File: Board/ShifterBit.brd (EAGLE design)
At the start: 27.2 x 61 mm, 13 parts

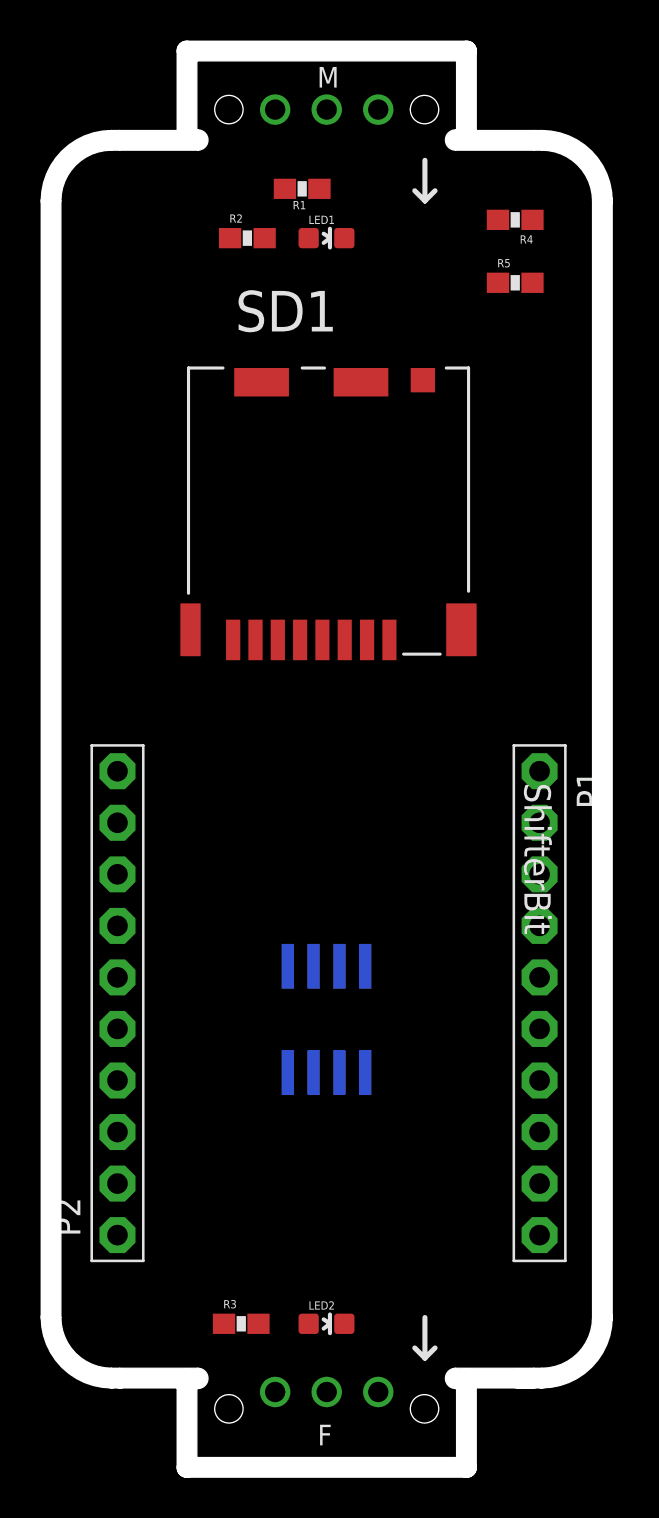
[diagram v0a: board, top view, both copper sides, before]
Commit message: corrected socket position
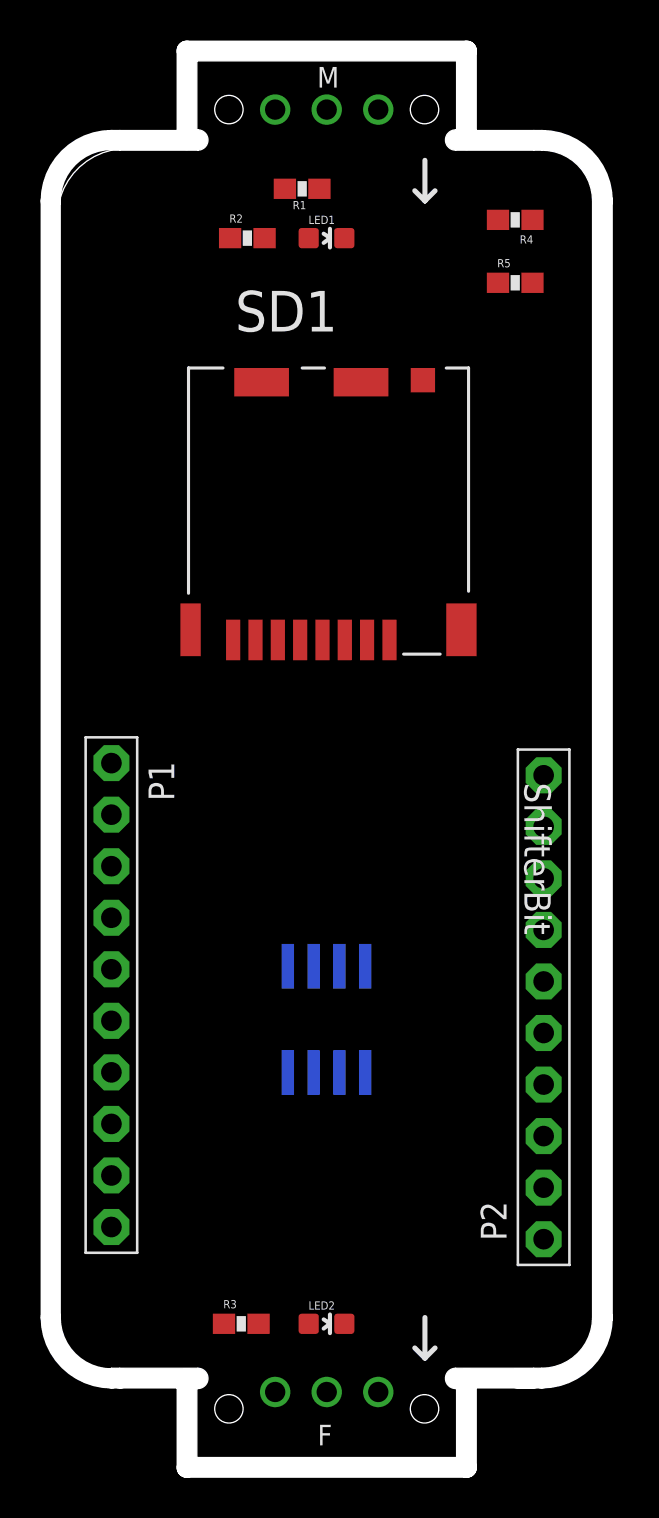
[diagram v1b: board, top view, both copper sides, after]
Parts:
- moved P1 21.1 mm to (2.60, 23.0)
- moved P2 21.0 mm to (23.9, 22.4)
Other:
- outline, holes or cut-outs redrawn
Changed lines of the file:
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@@
 <board>
 <plain>
-<wire x1="0.11" y1="62.135" x2="0.11" y2="7.11" width="0" layer="20"/>
-<wire x1="0.11" y1="7.11" x2="2.61" y2="4.61" width="0" layer="20" curve="90"/>
+<wire x1="0.01" y1="60.535" x2="0.01" y2="5.51" width="0" layer="20"/>
+<wire x1="0.01" y1="5.51" x2="2.61" y2="4.61" width="0" layer="20" curve="90"/>
 <wire x1="2.61" y1="4.61" x2="3.01" y2="4.61" width="0" layer="20"/>
-<wire x1="0.11" y1="62.135" x2="2.61" y2="64.635" width="0" layer="20" curve="-90"/>
+<wire x1="0.01" y1="60.535" x2="2.61" y2="64.635" width="0" layer="20" curve="-90"/>
 <wire x1="2.61" y1="64.635" x2="3.01" y2="64.635" width="0" layer="20"/>
 <wire x1="23.41" y1="64.635" x2="23.81" y2="64.635" width="0" layer="20"/>
@@
 <element name="BSF1" library="bitSnap" package="BITSNAP_V03_FEMALE" value="BITSNAP_V03_FEMALE" x="6.605" y="0" locked="yes"/>
 <element name="BSM1" library="bitSnap" package="BITSNAP_V03_MALE" value="BITSNAP_V03_MALE" x="19.815" y="69.245" rot="R180"/>
-<element name="P1" library="adafruit" package="1X10-BIG" value="" x="23.7" y="22.6" rot="R270"/>
-<element name="P2" library="adafruit" package="1X10-BIG" value="" x="2.9" y="22.6" rot="R90"/>
+<element name="P1" library="adafruit" package="1X10-BIG" value="" x="2.6" y="23" rot="R270"/>
+<element name="P2" library="adafruit" package="1X10-BIG" value="" x="23.9" y="22.4" rot="R90"/>
 <element name="SD1" library="HIROSE-DM3CS-SF" package="HIROSE_DM3CS-SF" value="" x="16.3" y="40.5">
 <attribute name="OC_NEWARK" value="35R0581" x="16.3" y="40.5" size="1.778" layer="27" display="off"/>
@@
 <wire x1="14.077" y1="6.8" x2="12.565" y2="19.1838" width="0" layer="19" extent="1-16"/>
 <wire x1="10.67" y1="3.44" x2="14.077" y2="6.8" width="0" layer="19" extent="1-1"/>
-<wire x1="23.7" y1="11.17" x2="14.077" y2="6.8" width="0" layer="19" extent="1-1"/>
-<wire x1="2.9" y1="11.17" x2="10.67" y2="3.44" width="0" layer="19" extent="1-1"/>
+<wire x1="2.6" y1="11.57" x2="14.077" y2="6.8" width="0" layer="19" extent="1-1"/>
+<wire x1="23.9" y1="10.97" x2="10.67" y2="3.44" width="0" layer="19" extent="1-1"/>
 </signal>
 <signal name="VCC">
@@
 <contactref element="R4" pad="1"/>
 <wire x1="23.35" y1="58.1" x2="23.35" y2="61.2" width="0" layer="19" extent="1-1"/>
-<wire x1="23.7" y1="31.49" x2="23.35" y2="58.1" width="0" layer="19" extent="1-1"/>
+<wire x1="2.6" y1="31.89" x2="23.35" y2="58.1" width="0" layer="19" extent="1-1"/>
 </signal>
 <signal name="EN">
@@
 <contactref element="P1" pad="4"/>
 <contactref element="DPOT1" pad="1"/>
-<wire x1="11.295" y1="24.4162" x2="23.7" y2="26.41" width="0" layer="19" extent="16-16"/>
+<wire x1="11.295" y1="24.4162" x2="2.6" y2="26.81" width="0" layer="19" extent="16-16"/>
 </signal>
 <signal name="D14">
@@
 <contactref element="DPOT1" pad="2"/>
 <wire x1="12.565" y1="24.4162" x2="11.9" y2="40.5" width="0" layer="19" extent="1-16"/>
-<wire x1="23.7" y1="23.87" x2="12.565" y2="24.4162" width="0" layer="19" extent="16-16"/>
+<wire x1="2.6" y1="24.27" x2="12.565" y2="24.4162" width="0" layer="19" extent="16-16"/>
 </signal>
 <signal name="D12">
 <contactref element="P1" pad="6"/>
 <contactref element="SD1" pad="7"/>
-<wire x1="23.7" y1="21.33" x2="9.7" y2="40.5" width="0" layer="19" extent="1-1"/>
+<wire x1="2.6" y1="21.73" x2="9.7" y2="40.5" width="0" layer="19" extent="1-1"/>
 </signal>
 <signal name="D13">
@@
 <contactref element="DPOT1" pad="3"/>
 <wire x1="13.835" y1="24.4162" x2="14.1" y2="40.5" width="0" layer="19" extent="1-16"/>
-<wire x1="23.7" y1="18.79" x2="13.835" y2="24.4162" width="0" layer="19" extent="16-16"/>
+<wire x1="2.6" y1="19.19" x2="13.835" y2="24.4162" width="0" layer="19" extent="16-16"/>
 </signal>
 <signal name="V+">
@@
 <contactref element="P2" pad="8"/>
 <contactref element="R2" pad="1"/>
-<wire x1="2.9" y1="28.95" x2="8.45" y2="60.3" width="0" layer="19" extent="1-1"/>
+<wire x1="23.9" y1="28.75" x2="8.45" y2="60.3" width="0" layer="19" extent="1-1"/>
 </signal>
 <signal name="D4">
 <contactref element="P2" pad="7"/>
 <contactref element="R3" pad="1"/>
-<wire x1="8.15" y1="6.8" x2="2.9" y2="26.41" width="0" layer="19" extent="1-1"/>
+<wire x1="8.15" y1="6.8" x2="23.9" y2="26.21" width="0" layer="19" extent="1-1"/>
 </signal>
 <signal name="D0">
@@
 <contactref element="P2" pad="4"/>
 <contactref element="SD1" pad="2"/>
-<wire x1="2.9" y1="18.79" x2="15.2" y2="40.5" width="0" layer="19" extent="1-1"/>
+<wire x1="23.9" y1="18.59" x2="15.2" y2="40.5" width="0" layer="19" extent="1-1"/>
 </signal>
 <signal name="3V">
@@
 <contactref element="DPOT1" pad="8"/>
 <wire x1="11.295" y1="19.1838" x2="13" y2="40.5" width="0" layer="19" extent="1-16"/>
-<wire x1="2.9" y1="16.25" x2="11.295" y2="19.1838" width="0" layer="19" extent="16-16"/>
+<wire x1="23.9" y1="16.05" x2="11.295" y2="19.1838" width="0" layer="19" extent="16-16"/>
 </signal>
 <signal name="LD0">

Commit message: added some aesthetics
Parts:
- R4: value 2K2 -> 3K3
- R5: value 560 -> 820
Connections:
- net 3V: no longer DPOT1.8
- net VCC: now also DPOT1.8
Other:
- outline, holes or cut-outs redrawn
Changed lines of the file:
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@@
 <layer number="47" name="Measures" color="7" fill="1" visible="yes" active="yes"/>
 <layer number="48" name="Document" color="7" fill="1" visible="yes" active="yes"/>
-<layer number="49" name="Reference" color="10" fill="1" visible="yes" active="yes"/>
+<layer number="49" name="Reference" color="10" fill="1" visible="no" active="yes"/>
 <layer number="50" name="dxf" color="7" fill="1" visible="yes" active="yes"/>
 <layer number="51" name="tDocu" color="6" fill="1" visible="yes" active="yes"/>
@@
 <board>
 <plain>
-<wire x1="0.01" y1="60.535" x2="0.01" y2="5.51" width="0" layer="20"/>
-<wire x1="0.01" y1="5.51" x2="2.61" y2="4.61" width="0" layer="20" curve="90"/>
-<wire x1="2.61" y1="4.61" x2="3.01" y2="4.61" width="0" layer="20"/>
-<wire x1="0.01" y1="60.535" x2="2.61" y2="64.635" width="0" layer="20" curve="-90"/>
+<wire x1="0.11" y1="62.035" x2="0.11" y2="6.81" width="0" layer="20"/>
+<wire x1="0.11" y1="6.81" x2="3.01" y2="4.61" width="0" layer="20" curve="90"/>
+<wire x1="0.11" y1="62.035" x2="2.61" y2="64.635" width="0" layer="20" curve="-90"/>
 <wire x1="2.61" y1="64.635" x2="3.01" y2="64.635" width="0" layer="20"/>
 <wire x1="23.41" y1="64.635" x2="23.81" y2="64.635" width="0" layer="20"/>
@@
 <element name="R2" library="SparkFun-Passives" package="0603-RES" value="56" x="9.3" y="60.3"/>
 <element name="R3" library="SparkFun-Passives" package="0603-RES" value="56" x="9" y="6.8"/>
-<element name="R4" library="SparkFun-Passives" package="0603-RES" value="2K2" x="22.5" y="61.2" rot="R180"/>
-<element name="R5" library="SparkFun-Passives" package="0603-RES" value="560" x="22.5" y="58.1"/>
+<element name="R4" library="SparkFun-Passives" package="0603-RES" value="3K3" x="22.5" y="61.2" rot="R180"/>
+<element name="R5" library="SparkFun-Passives" package="0603-RES" value="820" x="22.5" y="58.1"/>
 <element name="DPOT1" library="SparkFun-AnalogIC" package="SO08" value="MCP41XXX" x="13.2" y="21.8" rot="MR180"/>
 </elements>
@@
 <contactref element="BSF1" pad="VCC"/>
 <contactref element="DPOT1" pad="5"/>
+<contactref element="DPOT1" pad="8"/>
 <wire x1="15.105" y1="19.1838" x2="15.75" y2="66.635" width="0" layer="19" extent="16-16"/>
+<wire x1="11.295" y1="19.1838" x2="15.105" y2="19.1838" width="0" layer="19" extent="16-16"/>
 <wire x1="15.75" y1="3.44" x2="15.105" y2="19.1838" width="0" layer="19" extent="16-16"/>
 </signal>
@@
 <contactref element="P2" pad="3"/>
 <contactref element="SD1" pad="4"/>
-<contactref element="DPOT1" pad="8"/>
-<wire x1="11.295" y1="19.1838" x2="13" y2="40.5" width="0" layer="19" extent="1-16"/>
-<wire x1="23.9" y1="16.05" x2="11.295" y2="19.1838" width="0" layer="19" extent="16-16"/>
+<wire x1="23.9" y1="16.05" x2="13" y2="40.5" width="0" layer="19" extent="1-1"/>
 </signal>
 <signal name="LD0">

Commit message: renamed signal
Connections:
- net A renamed A1
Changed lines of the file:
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@@
 <contactref element="P1" pad="1"/>
 </signal>
-<signal name="A">
+<signal name="A1">
 <contactref element="P1" pad="2"/>
 <contactref element="R5" pad="2"/>

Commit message: removed unused nets
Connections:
- removed net D0: P2.6
- removed net D2: P2.5
- removed net EN: P1.3
- removed net LD0: P2.2
- removed net RST: P1.1
- removed net RX: P2.9
- removed net TX: P2.10
- removed net V+: P1.8
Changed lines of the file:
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@@
 <wire x1="13.21" y1="66.635" x2="12.85" y2="62.73" width="0" layer="19" extent="1-1"/>
-</signal>
-<signal name="RST">
-<contactref element="P1" pad="1"/>
 </signal>
 <signal name="A1">
@@
 <wire x1="23.35" y1="58.1" x2="23.35" y2="61.2" width="0" layer="19" extent="1-1"/>
 <wire x1="2.6" y1="31.89" x2="23.35" y2="58.1" width="0" layer="19" extent="1-1"/>
-</signal>
-<signal name="EN">
-<contactref element="P1" pad="3"/>
 </signal>
 <signal name="D16">
@@
 <wire x1="2.6" y1="19.19" x2="13.835" y2="24.4162" width="0" layer="19" extent="16-16"/>
 </signal>
-<signal name="V+">
-<contactref element="P1" pad="8"/>
-</signal>
 <signal name="VBAT">
 <contactref element="P1" pad="9"/>
-</signal>
-<signal name="TX">
-<contactref element="P2" pad="10"/>
-</signal>
-<signal name="RX">
-<contactref element="P2" pad="9"/>
 </signal>
 <signal name="D5">
@@
 <wire x1="8.15" y1="6.8" x2="23.9" y2="26.21" width="0" layer="19" extent="1-1"/>
 </signal>
-<signal name="D0">
-<contactref element="P2" pad="6"/>
-</signal>
-<signal name="D2">
-<contactref element="P2" pad="5"/>
-</signal>
 <signal name="D15">
 <contactref element="P2" pad="4"/>
@@
 <wire x1="23.9" y1="16.05" x2="13" y2="40.5" width="0" layer="19" extent="1-1"/>
 </signal>
-<signal name="LD0">
-<contactref element="P2" pad="2"/>
-</signal>
 <signal name="N$4">

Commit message: repositioned elements
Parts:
- moved DPOT1 1.22 mm to (13.4, 23.0)
- moved R5 1.17 mm to (21.4, 58.5)
- moved R4 1.14 mm to (21.4, 60.9)
- moved R2 1.06 mm to (8.60, 59.5)
- moved SD1 1.02 mm to (16.1, 41.5)
- moved LED1 0.81 mm to (13.3, 59.5)
- moved P2 0.78 mm to (23.4, 23.0)
- moved LED2 0.70 mm to (13.2, 7.50)
- moved R3 0.70 mm to (9.00, 7.50)
- moved P1 0.50 mm to (3.10, 23.0)
- moved R1 0.50 mm to (12.0, 62.2)

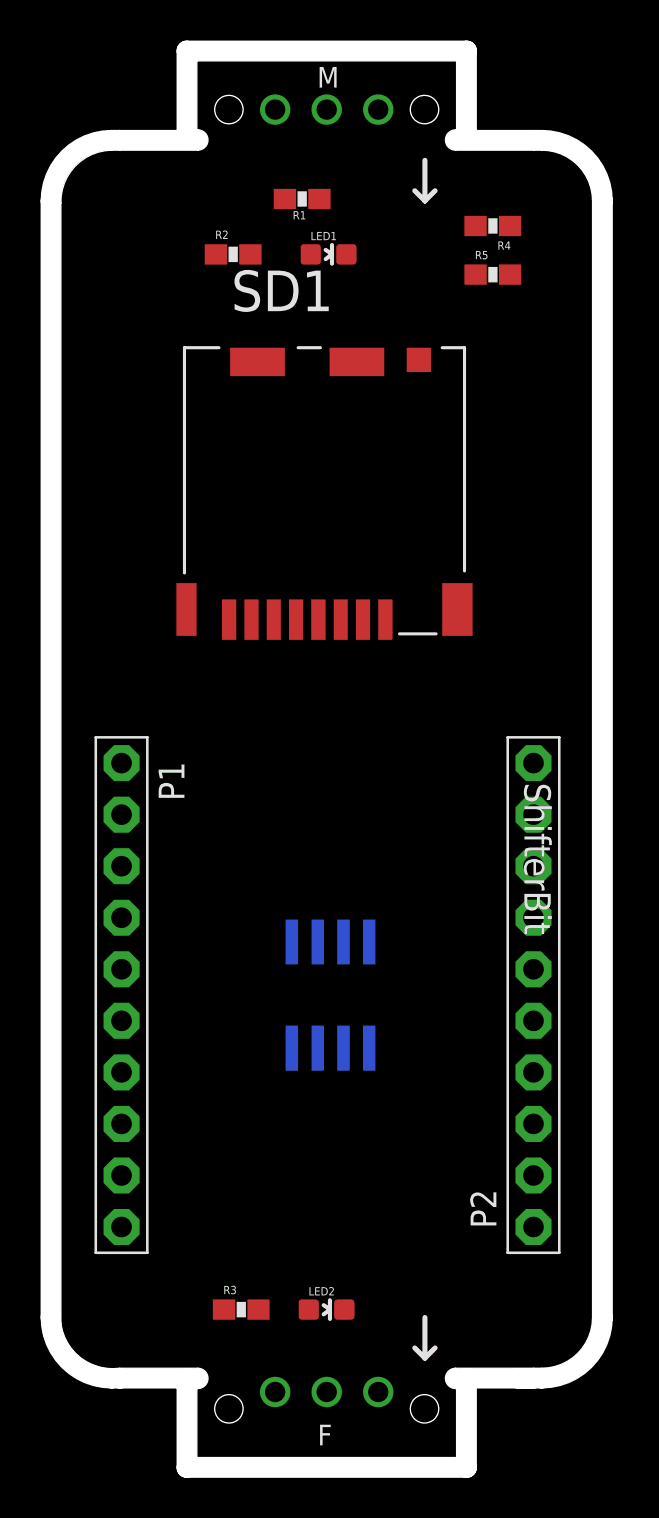
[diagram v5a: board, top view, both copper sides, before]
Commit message: load sparkfun design rules and auto route
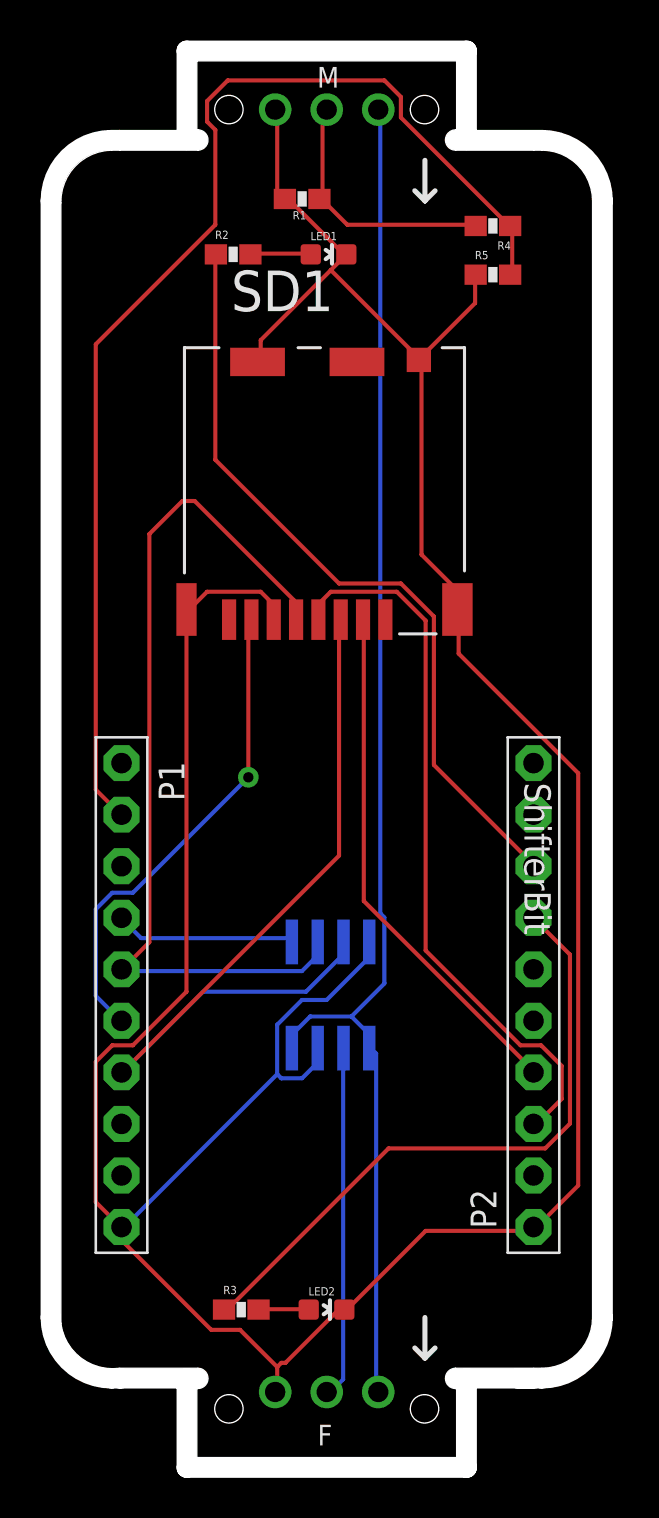
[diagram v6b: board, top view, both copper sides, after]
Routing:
- net GND: track 0.00 -> 164.7 mm
- net VCC: track 0.00 -> 68.5 mm
- net A1: track 0.00 -> 59.7 mm
- net D14: track 0.00 -> 43.6 mm
- net D13: track 0.00 -> 40.8 mm
- net D5: track 0.00 -> 38.4 mm
- net 3V: track 0.00 -> 35.7 mm
- net D4: track 0.00 -> 31.7 mm
- net D15: track 0.00 -> 25.8 mm
- net D12: track 0.00 -> 24.1 mm, vias 0 -> 1
- net SIG_OUT: track 0.00 -> 17.4 mm
- net SIG_IN: track 0.00 -> 12.8 mm
- net D16: track 0.00 -> 8.93 mm
- net N$4: track 0.00 -> 3.00 mm
- net N$9: track 0.00 -> 2.48 mm

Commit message: grounded cd
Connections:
- net GND: now also SD1.11
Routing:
- net GND: track 164.7 -> 167.8 mm
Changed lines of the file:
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@@
 <wire x1="19.7104" y1="41.8592" x2="19.65" y2="42" width="0.2032" layer="1"/>
 <wire x1="23.5712" y1="11.5824" x2="23.4" y2="11.57" width="0.2032" layer="1"/>
+<contactref element="SD1" pad="11"/>
+<wire x1="14.7" y1="54.2" x2="17.75" y2="54.2" width="0.254" layer="1"/>
+<wire x1="17.75" y1="54.2" x2="17.75" y2="54.3" width="0.254" layer="1"/>
 </signal>
 <signal name="VCC">
